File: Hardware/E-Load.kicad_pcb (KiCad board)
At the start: 2 copper layers, 63.5 x 71.1 mm, 64 parts, among them J1 Barrel_Jack, J2 Conn_01x05_Male, J3 Conn_01x08_Male, J4 Screw_Terminal_01x03, Q1 BUK7M45-40EX, SW2 SW_Push, SW3 SW_Push, SW4 SW_Push, U1 AP2210K-3.3, U2 STM32F103C8Tx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

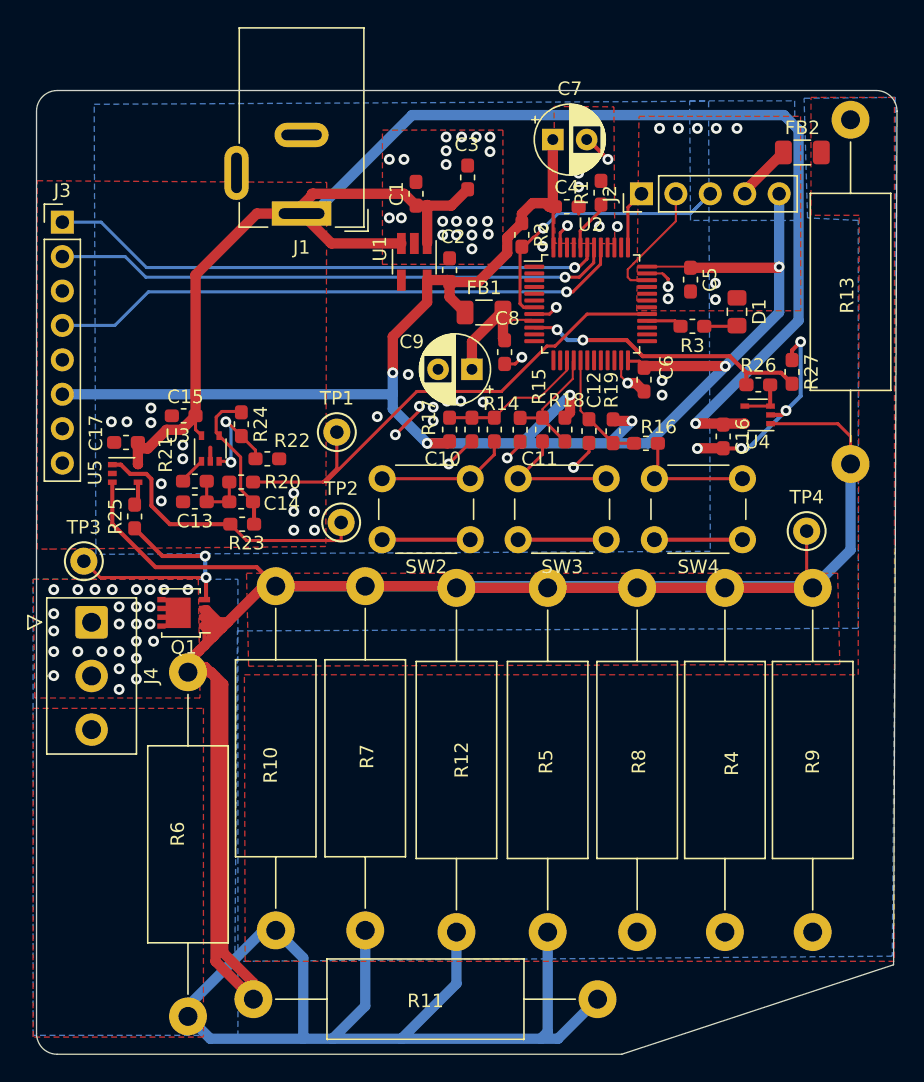
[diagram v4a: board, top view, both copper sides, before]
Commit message: Added ADC instead of opamp. Added stiching
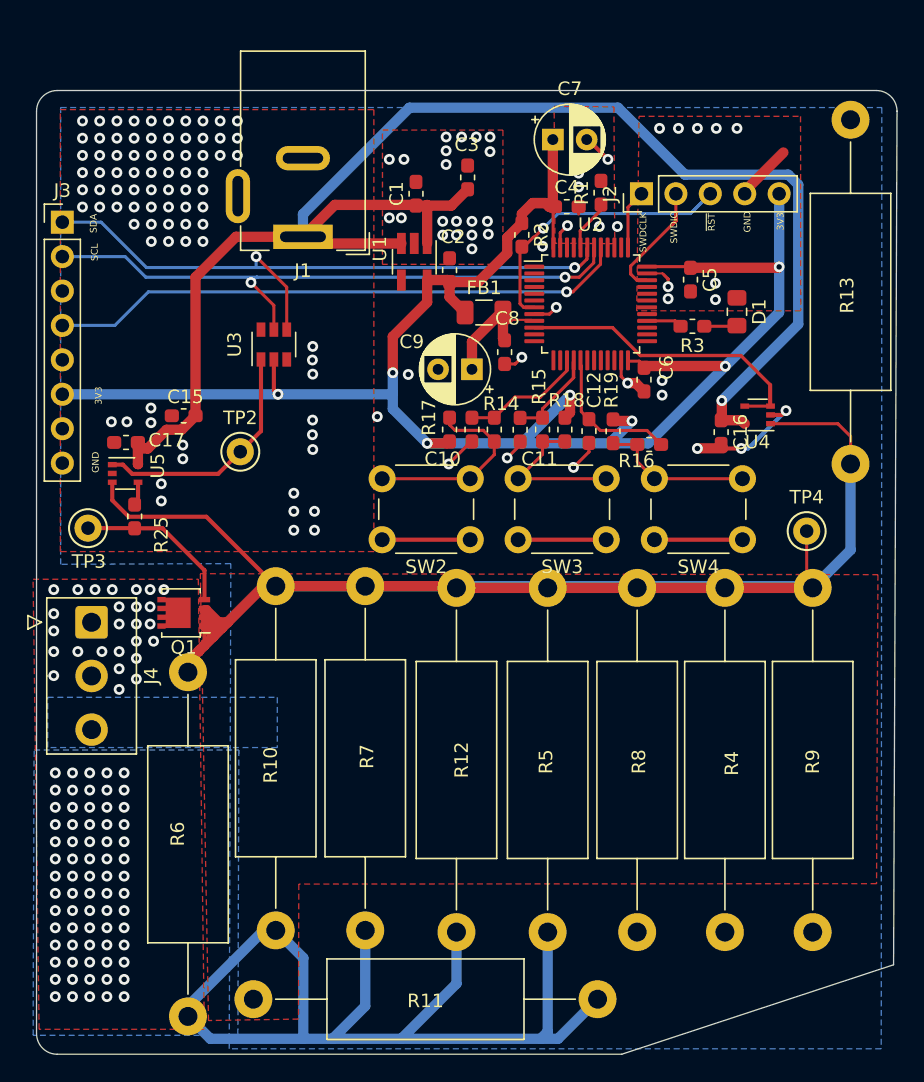
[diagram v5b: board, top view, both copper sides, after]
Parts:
- removed C13: 1n, Capacitor_SMD:C_0603_1608Metric_Pad1.05x0.95mm_HandSolder
- removed C14: 470p, Capacitor_SMD:C_0603_1608Metric_Pad1.05x0.95mm_HandSolder
- removed FB2: Ferrite_Bead, Capacitor_SMD:C_1206_3216Metric
- removed R20: 25.5k, Resistor_SMD:R_0603_1608Metric_Pad1.05x0.95mm_HandSolder
- removed R21: 21k, Resistor_SMD:R_0603_1608Metric_Pad1.05x0.95mm_HandSolder
- removed R22: 23.2k, Resistor_SMD:R_0603_1608Metric_Pad1.05x0.95mm_HandSolder
- removed R23: 50, Resistor_SMD:R_0603_1608Metric_Pad1.05x0.95mm_HandSolder
- removed R24: 46.4k, Resistor_SMD:R_0603_1608Metric_Pad1.05x0.95mm_HandSolder
- removed R26: 20k, Resistor_SMD:R_0603_1608Metric_Pad1.05x0.95mm_HandSolder
- removed R27: 10k, Resistor_SMD:R_0603_1608Metric_Pad1.05x0.95mm_HandSolder
- removed TP1: TestPoint_Alt, TestPoint:TestPoint_Keystone_5000-5004_Miniature
- J1: value Barrel_Jack -> Barrel_Jack_Switch
- U3: value TLV172IDCK -> DAC121C081CIMK; footprint Package_TO_SOT_SMD:SOT-353_SC-70-5 -> Package_TO_SOT_SMD:SOT-23-6
- moved TP2 9.09 mm to (157.3, 86.1)
- moved U3 8.99 mm to (159.8, 78.2)
- moved TP3 2.46 mm to (146.0, 91.7)
- moved J1 1.72 mm to (161.9, 70.2)
- moved C16 0.35 mm to (192.8, 84.6)
- moved R16 0.25 mm to (187.5, 85.6), turned to 180 degrees
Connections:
- J1 pad 3: (no net) -> GND
- J3 pad 1: /MCU/SDA -> /CurrentControl/SDA
- J3 pad 2: /MCU/SCL -> /CurrentControl/SCL
- J4 pad 3: GNDA -> GND
- R10 pad 2: GNDA -> GND
- R11 pad 2: GNDA -> GND
- R12 pad 2: GNDA -> GND
- R13 pad 2: GNDA -> GND
- R17 pad 1: /Buttons/BUTT_A -> Net-(R14-Pad2)
- R18 pad 1: /Buttons/BUTT_B -> Net-(R15-Pad2)
- R19 pad 1: /Buttons/BUTT_C -> Net-(R16-Pad2)
- R4 pad 2: GNDA -> GND
- R5 pad 2: GNDA -> GND
- R6 pad 2: GNDA -> GND
- R7 pad 2: GNDA -> GND
- R8 pad 2: GNDA -> GND
- R9 pad 2: GNDA -> GND
- TP2 pad 1: Net-(R23-Pad1) -> Net-(TP2-Pad1)
- U2 pad 29: /CurrentControl/PWM -> (no net)
- U2 pad 42: /MCU/SCL -> /CurrentControl/SCL
- U2 pad 43: /MCU/SDA -> /CurrentControl/SDA
- U3 pad 1: Net-(R21-Pad2) -> Net-(TP2-Pad1)
- U3 pad 2: GND -> +3V3
- U3 pad 3: Net-(R22-Pad2) -> GND
- U3 pad 4: Net-(C14-Pad1) -> /CurrentControl/SDA
- U3 pad 5: +12V -> /CurrentControl/SCL
- U4 pad 3: Net-(R26-Pad2) -> /CurrentControl/ADC
- U4 pad 4: Net-(R26-Pad2) -> /CurrentControl/ADC
- U5 pad 1: Net-(R23-Pad1) -> Net-(TP2-Pad1)
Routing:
- net GNDA: track 77.5 -> 0.00 mm
- net GND: track 64.0 -> 130.5 mm, vias 70 -> 131
- net /CurrentControl/Vmeas: track 191.5 -> 135.7 mm
- net /CurrentControl/SDA: track 0.00 -> 48.3 mm, vias 0 -> 2
- net /CurrentControl/SCL: track 0.00 -> 46.2 mm, vias 0 -> 2
- net /MCU/SCL: track 41.3 -> 0.00 mm, vias 1 -> 0
- net /MCU/SDA: track 41.1 -> 0.00 mm, vias 1 -> 0
- net /CurrentControl/PWM: track 38.3 -> 0.00 mm
- net Net-(R23-Pad1): track 21.7 -> 0.00 mm
- net Net-(TP2-Pad1): track 0.00 -> 17.8 mm
- net Net-(C14-Pad1): track 11.1 -> 0.00 mm
- net Net-(R22-Pad2): track 7.73 -> 0.00 mm, vias 2 -> 0
- net +12V: track 123.0 -> 116.0 mm
- net Net-(Q1-Pad4): track 18.9 -> 12.0 mm, vias 2 -> 0
- net Net-(C13-Pad1): track 4.65 -> 0.00 mm
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- removed copper zone on B.Cu, net GNDA
- removed copper zone on F.Cu, net GNDA
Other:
- board text added: "3V3"
- board text added: "GND"
- board text added: "SCL"
- board text added: "SDA"
- board text added: "SWDCLK"
- board text added: "SWDIO"
- board text added: "~RST"

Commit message: Minor changes
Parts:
- added R20: 1k, Resistor_SMD:R_0603_1608Metric_Pad1.05x0.95mm_HandSolder, F.Cu at (159.6, 84.2)
- J1: value Barrel_Jack_Switch -> PJ-002A
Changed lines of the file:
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@@
     (tracks 548)
     (zones 0)
-    (modules 53)
+    (modules 54)
     (nets 26)
   )
@@
       (linewidth 0.100000)
       (plotframeref false)
-      (viasonmask false)
+      (viasonmask true)
       (mode 1)
       (useauxorigin false)
@@
       (outputformat 1)
       (mirror false)
-      (drillshape 1)
+      (drillshape 0)
       (scaleselection 1)
-      (outputdirectory ""))
+      (outputdirectory "./CAMFILES"))
   )
   (net 0 "")
@@
   (net 23 /CurrentControl/SCL)
   (net 24 /CurrentControl/SDA)
-  (net 25 "Net-(TP2-Pad1)")
+  (net 25 "Net-(R20-Pad2)")
   (net_class Default "This is the default net class."
     (clearance 0.1778)
@@
     (add_net GND)
     (add_net "Net-(D1-Pad2)")
+    (add_net "Net-(J3-Pad3)")
+    (add_net "Net-(J3-Pad5)")
+    (add_net "Net-(J3-Pad7)")
+    (add_net "Net-(J4-Pad2)")
     (add_net "Net-(Q1-Pad4)")
     (add_net "Net-(R1-Pad1)")
@@
     (add_net "Net-(R15-Pad2)")
     (add_net "Net-(R16-Pad2)")
+    (add_net "Net-(R20-Pad2)")
     (add_net "Net-(R25-Pad2)")
     (add_net "Net-(R3-Pad2)")
-    (add_net "Net-(TP2-Pad1)")
+    (add_net "Net-(U1-Pad4)")
+    (add_net "Net-(U2-Pad1)")
+    (add_net "Net-(U2-Pad11)")
+    (add_net "Net-(U2-Pad12)")
+    (add_net "Net-(U2-Pad13)")
+    (add_net "Net-(U2-Pad14)")
+    (add_net "Net-(U2-Pad18)")
+    (add_net "Net-(U2-Pad19)")
+    (add_net "Net-(U2-Pad2)")
+    (add_net "Net-(U2-Pad20)")
+    (add_net "Net-(U2-Pad21)")
+    (add_net "Net-(U2-Pad22)")
+    (add_net "Net-(U2-Pad25)")
+    (add_net "Net-(U2-Pad26)")
+    (add_net "Net-(U2-Pad27)")
+    (add_net "Net-(U2-Pad29)")
+    (add_net "Net-(U2-Pad3)")
+    (add_net "Net-(U2-Pad30)")
+    (add_net "Net-(U2-Pad31)")
+    (add_net "Net-(U2-Pad32)")
+    (add_net "Net-(U2-Pad33)")
+    (add_net "Net-(U2-Pad38)")
+    (add_net "Net-(U2-Pad39)")
+    (add_net "Net-(U2-Pad4)")
+    (add_net "Net-(U2-Pad40)")
+    (add_net "Net-(U2-Pad45)")
+    (add_net "Net-(U2-Pad46)")
+    (add_net "Net-(U2-Pad5)")
+    (add_net "Net-(U2-Pad6)")
+    (add_net "Net-(U3-Pad6)")
     (add_net VCC)
     (add_net VDDA)
+  )
+  (module Resistor_SMD:R_0603_1608Metric_Pad1.05x0.95mm_HandSolder (layer F.Cu)
+    (at 159.639 84.1883 180)
+    (descr "Resistor SMD 0603 (1608 Metric), square (rectangular) end terminal, IPC_7351 nominal with elongated pad for handsoldering. (Body size source: http://www.tortai-tech.com/upload/download/2011102023233369053.pdf), generated with kicad-footprint-generator")
+    (tags "resistor handsolder")
+    (attr smd)
+    (fp_text reference R20 (at 0 -1.43) (layer F.SilkS)
+      (effects (font (size 1 1) (thickness 0.15)))
+    )
+    (fp_text value 1k (at 0 1.43) (layer F.Fab)
+      (effects (font (size 1 1) (thickness 0.15)))
+    )
+    (fp_text user %R (at 0 0) (layer F.Fab)
+      (effects (font (size 0.4 0.4) (thickness 0.06)))
+    )
+    (fp_line (start -0.8 0.4) (end -0.8 -0.4) (layer F.Fab) (width 0.1))
+    (fp_line (start -0.8 -0.4) (end 0.8 -0.4) (layer F.Fab) (width 0.1))
+    (fp_line (start 0.8 -0.4) (end 0.8 0.4) (layer F.Fab) (width 0.1))
+    (fp_line (start 0.8 0.4) (end -0.8 0.4) (layer F.Fab) (width 0.1))
+    (fp_line (start -0.171267 -0.51) (end 0.171267 -0.51) (layer F.SilkS) (width 0.12))
+    (fp_line (start -0.171267 0.51) (end 0.171267 0.51) (layer F.SilkS) (width 0.12))
+    (fp_line (start -1.65 0.73) (end -1.65 -0.73) (layer F.CrtYd) (width 0.05))
+    (fp_line (start -1.65 -0.73) (end 1.65 -0.73) (layer F.CrtYd) (width 0.05))
+    (fp_line (start 1.65 -0.73) (end 1.65 0.73) (layer F.CrtYd) (width 0.05))
+    (fp_line (start 1.65 0.73) (end -1.65 0.73) (layer F.CrtYd) (width 0.05))
+    (pad 2 smd roundrect (at 0.875 0 180) (size 1.05 0.95) (layers F.Cu F.Paste F.Mask) (roundrect_rratio 0.25)
+      (net 25 "Net-(R20-Pad2)"))
+    (pad 1 smd roundrect (at -0.875 0 180) (size 1.05 0.95) (layers F.Cu F.Paste F.Mask) (roundrect_rratio 0.25)
+      (net 1 GND))
+    (model ${KISYS3DMOD}/Resistor_SMD.3dshapes/R_0603_1608Metric.wrl
+      (at (xyz 0 0 0))
+      (scale (xyz 1 1 1))
+      (rotate (xyz 0 0 0))
+    )
   )
   (module Connector_BarrelJack:BarrelJack_Wuerth_6941xx301002 (layer F.Cu)
@@
       (effects (font (size 1 1) (thickness 0.15)))
     )
-    (fp_text value Barrel_Jack_Switch (at 0 15.5) (layer F.Fab)
+    (fp_text value PJ-002A (at 0 15.5) (layer F.Fab)
       (effects (font (size 1 1) (thickness 0.15)))
     )
@@
       (net 3 +3V3))
     (pad 1 smd rect (at -1.1 -0.95 90) (size 1.06 0.65) (layers F.Cu F.Paste F.Mask)
-      (net 25 "Net-(TP2-Pad1)"))
+      (net 25 "Net-(R20-Pad2)"))
     (model ${KISYS3DMOD}/Package_TO_SOT_SMD.3dshapes/SOT-23-6.wrl
       (at (xyz 0 0 0))
@@
     )
     (pad 1 thru_hole circle (at 0 0) (size 2 2) (drill 1) (layers *.Cu *.Mask)
-      (net 25 "Net-(TP2-Pad1)"))
+      (net 25 "Net-(R20-Pad2)"))
     (model ${KISYS3DMOD}/TestPoint.3dshapes/TestPoint_Keystone_5000-5004_Miniature.wrl
       (at (xyz 0 0 0))
@@
       (net 20 /CurrentControl/Vmeas))
     (pad 1 smd rect (at -0.95 -0.65) (size 0.65 0.4) (layers F.Cu F.Paste F.Mask)
-      (net 25 "Net-(TP2-Pad1)"))
+      (net 25 "Net-(R20-Pad2)"))
     (model ${KISYS3DMOD}/Package_TO_SOT_SMD.3dshapes/SOT-353_SC-70-5.wrl
       (at (xyz 0 0 0))

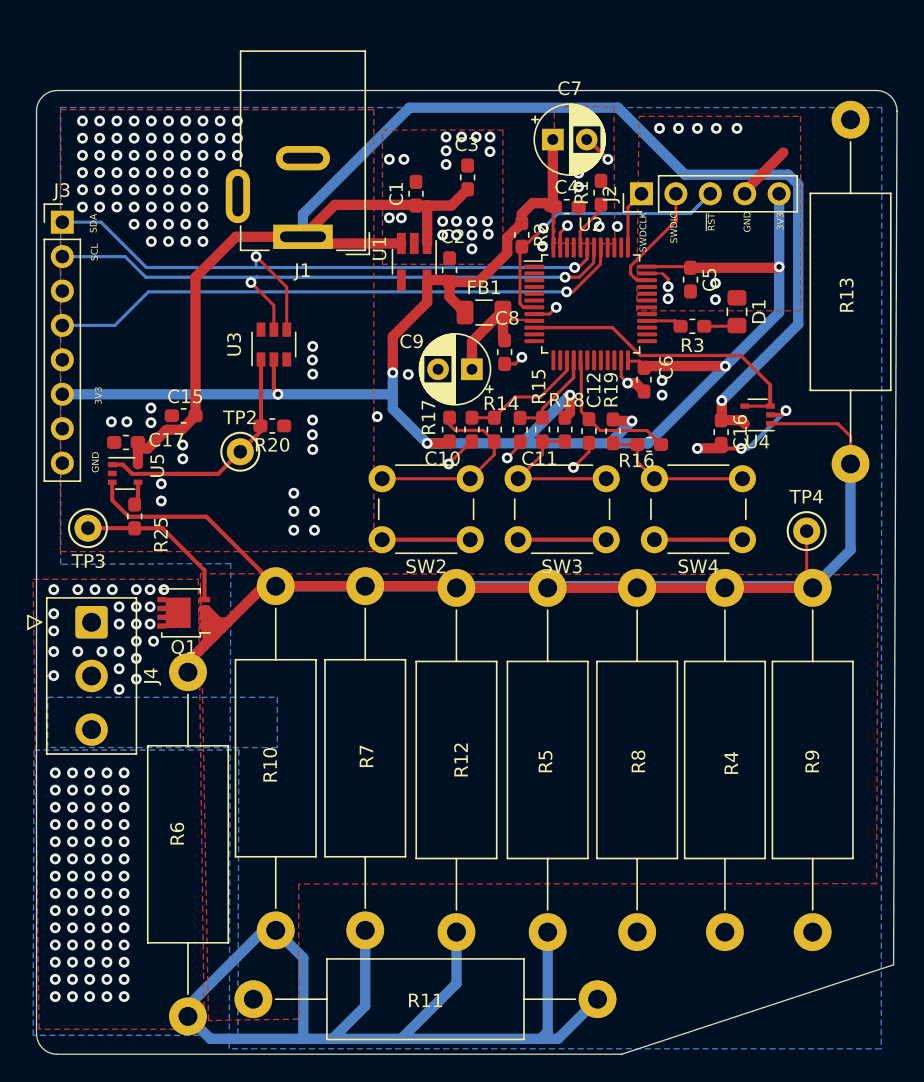
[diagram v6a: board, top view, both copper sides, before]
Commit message: Added pull up resistors on I2C line, added BOM
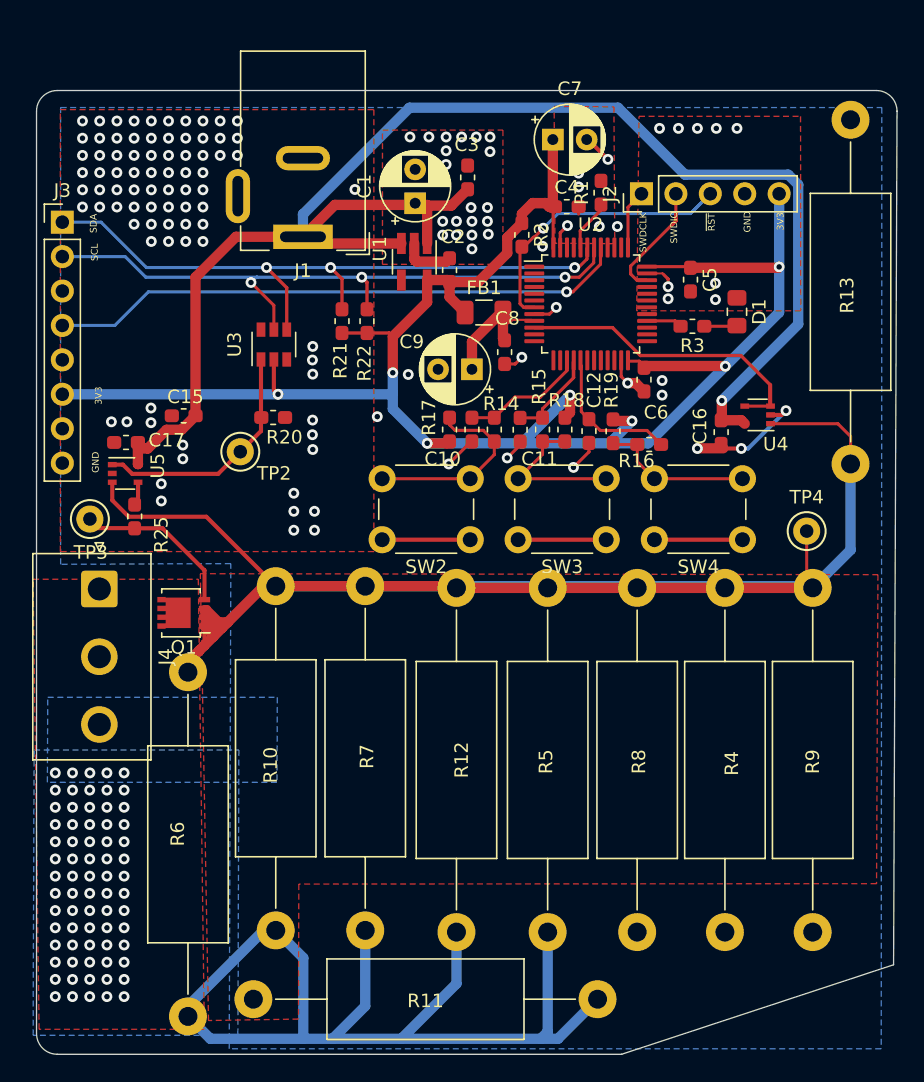
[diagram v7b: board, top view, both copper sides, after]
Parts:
- added R21: 1k, Resistor_SMD:R_0603_1608Metric_Pad1.05x0.95mm_HandSolder, F.Cu at (164.8, 76.5)
- added R22: 1k, Resistor_SMD:R_0603_1608Metric_Pad1.05x0.95mm_HandSolder, F.Cu at (166.6, 76.5)
- C1: footprint Capacitor_SMD:C_0603_1608Metric_Pad1.05x0.95mm_HandSolder -> Capacitor_THT:CP_Radial_D5.0mm_P2.50mm
- J4: footprint Connector_TE-Connectivity:TE_826576-3_1x03_P3.96mm_Vertical -> Connector_JST:JST_NV_B03P-NV_1x03_P5.00mm_Vertical
- moved J4 2.53 mm to (146.9, 96.2)
- moved C1 0.70 mm to (170.2, 67.8)
- moved TP3 0.69 mm to (146.2, 91.1)
- moved R20 0.63 mm to (159.7, 83.6)
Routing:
- net +3V3: track 136.7 -> 140.6 mm
- net /CurrentControl/SCL: track 46.2 -> 48.7 mm, vias 2 -> 3
- net /CurrentControl/SDA: track 48.3 -> 49.8 mm, vias 2 -> 3
- net GND: track 130.5 -> 130.4 mm, vias 131 -> 132
- net VCC: vias 96 -> 70
